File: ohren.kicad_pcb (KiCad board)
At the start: 2 copper layers, 60 x 28.7 mm, 34 parts, among them J1 Conn_01x14_Male, U1 TLC5951RHA, U2 TLC5951RHA

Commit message: Reroute finised
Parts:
- removed C4: CP, Capacitor_Tantalum_SMD:CP_EIA-6032-28_Kemet-C
- C10, C9: value CP -> C; footprint Capacitor_Tantalum_SMD:CP_EIA-6032-28_Kemet-C -> Capacitor_SMD:C_1206_3216Metric
- J1: value Conn_01x14_Male -> Conn_01x18_Male; footprint catear-pcb:solder_conn14 -> catear-pcb:solder_conn18
- moved C1 35.2 mm to (140.4, 107.9), turned to 270 degrees
- moved C3 28.1 mm to (138.4, 107.9), turned to 270 degrees
- moved C10 24.0 mm to (160.5, 112.6), turned to 180 degrees
- moved C9 15.1 mm to (128.0, 100.9)
- moved C6 13.8 mm to (145.6, 96.3), turned to 225 degrees
- moved C8 11.9 mm to (152.8, 102.3), turned to 225 degrees
- moved C7 10.7 mm to (135.4, 95.7)
- moved C5 8.68 mm to (122.9, 106.2)
- moved J1 3.55 mm to (139.2, 111.9), turned to 0 degrees
- turned D15 to 315 degrees
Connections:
- D19 pad 1: Net-(D19-Pad1) -> /U2_B4
- D20 pad 1: Net-(D20-Pad1) -> /U2_R4
- D21 pad 1: Net-(D21-Pad1) -> /U2_R1
- D23 pad 1: Net-(D23-Pad1) -> /U2_G1
- J1 pad 1: GND -> VCC
- J1 pad 10: /GSSIN -> /GSSCK
- J1 pad 11: /DCSIN -> /GSLAT
- J1 pad 12: GND -> /GSCKB
- J1 pad 13: VCC -> /DCSOUT
- J1 pad 14: VCC -> /GSSOUT
- J1 pad 2: /XBLNK -> VCC
- J1 pad 3: /DCSCK -> GND
- J1 pad 4: /GSSCK -> GND
- J1 pad 5: /GSLAT -> VDD
- J1 pad 6: /GSCKB -> /XBLNK
- J1 pad 7: VDD -> /DCSCK
- J1 pad 8: /DCSOUT -> /DCSIN
- J1 pad 9: /GSSOUT -> /GSSIN
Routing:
- net VCC: track 0.00 -> 157.2 mm, vias 0 -> 14
- net (no net): track 82.9 -> 0.00 mm, vias 4 -> 0
- net /U2_B6: track 0.00 -> 24.2 mm, vias 0 -> 1
- net /U2_G6: track 0.00 -> 22.8 mm, vias 0 -> 1
- net /U2_R6: track 0.00 -> 21.0 mm, vias 0 -> 1
- net /U2_G7: track 0.00 -> 15.2 mm, vias 0 -> 1
- net /U2_B5: track 0.00 -> 14.4 mm, vias 0 -> 1
- net /GSSOUT: track 0.00 -> 14.4 mm, vias 0 -> 1
- net /U2_B7: track 0.00 -> 13.7 mm, vias 0 -> 1
- net /U2_G5: track 0.00 -> 13.5 mm, vias 0 -> 1
- net /U2_R4: track 0.00 -> 13.5 mm, vias 0 -> 1
- net /DCSOUT: track 0.00 -> 13.2 mm, vias 0 -> 1
- net /U2_R5: track 0.00 -> 11.7 mm, vias 0 -> 1
- net /U2_R7: track 0.00 -> 11.6 mm, vias 0 -> 1
- net /GSSIN: track 0.00 -> 8.84 mm
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
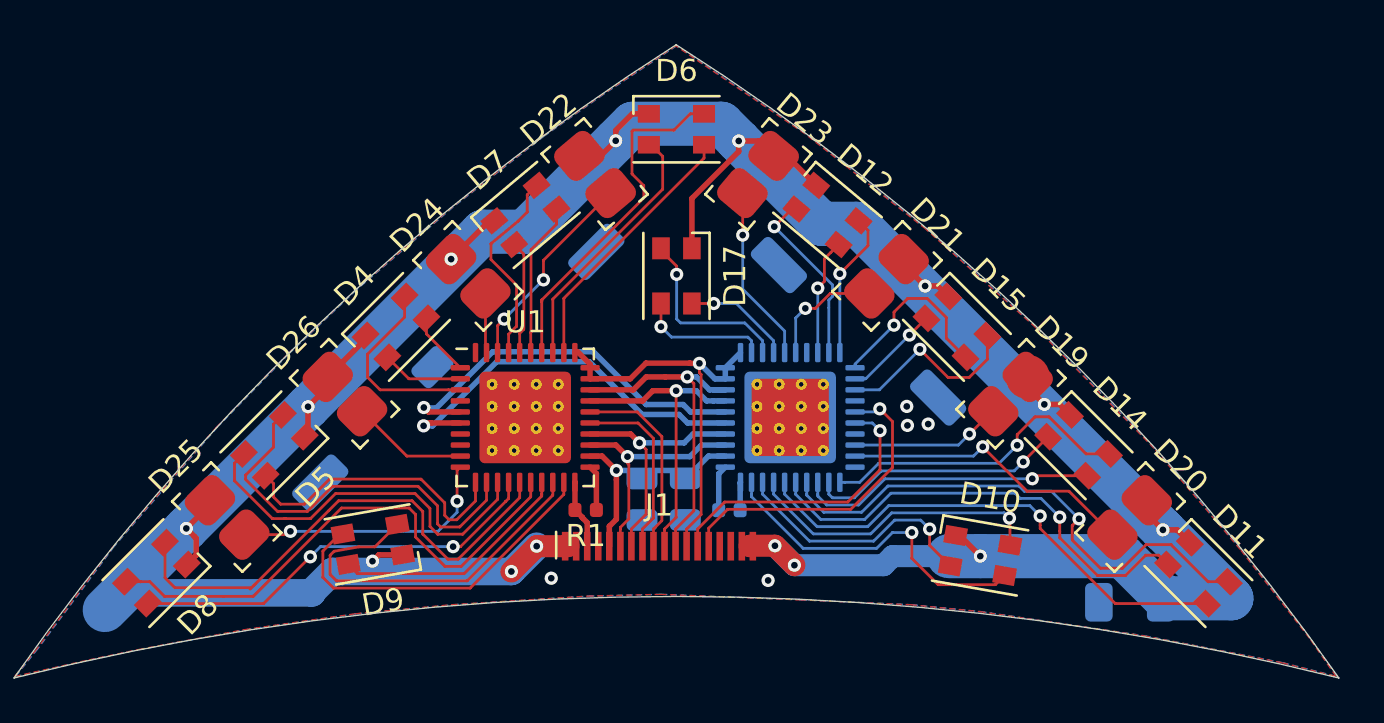
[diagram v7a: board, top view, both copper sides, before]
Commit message: Add additional VIA stitching and bypass capacitance
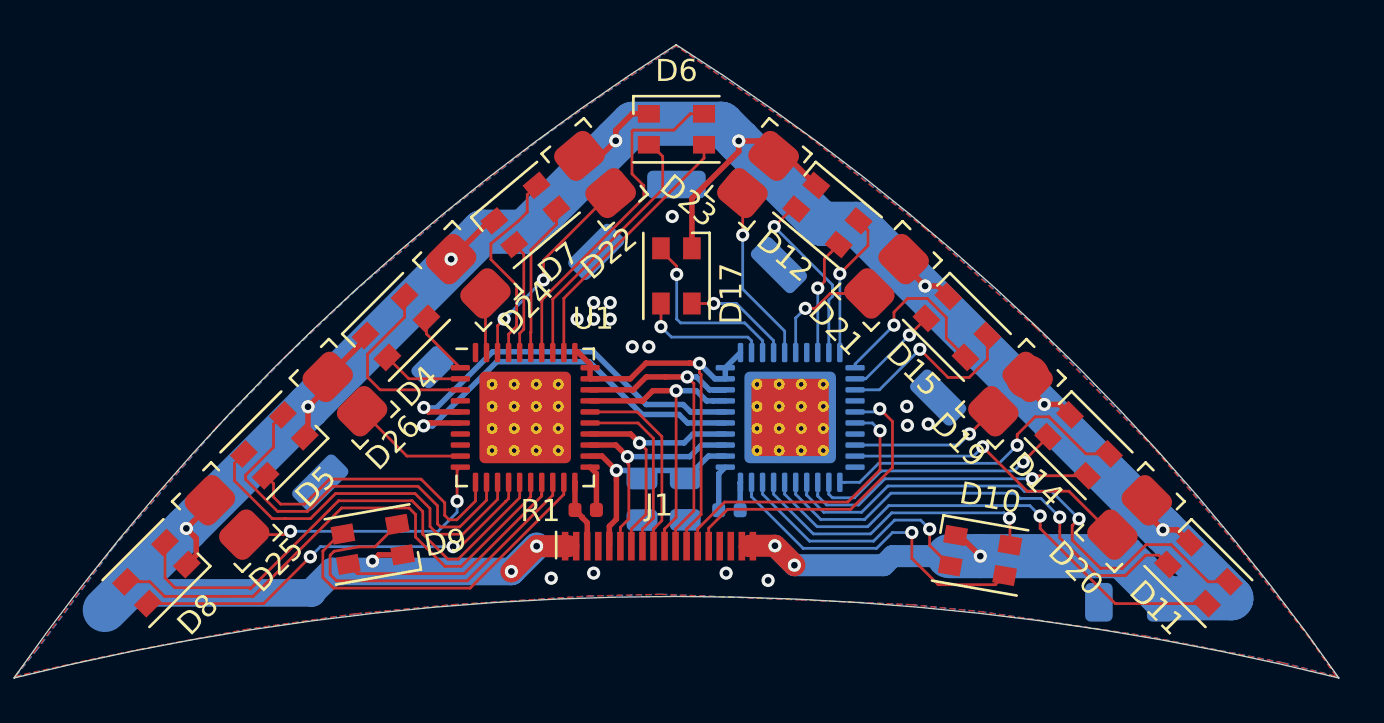
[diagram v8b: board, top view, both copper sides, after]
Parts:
- added C2: C, Capacitor_SMD:C_1210_3225Metric, B.Cu at (140.0, 92.2)
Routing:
- net GND: vias 5 -> 15
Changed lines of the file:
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@@
     (thickness 1.6)
     (drawings 9)
-    (tracks 605)
+    (tracks 615)
     (zones 0)
-    (modules 33)
+    (modules 34)
     (nets 69)
   )
@@
     (40 Dwgs.User user)
     (41 Cmts.User user)
-    (42 Eco1.User user hide)
-    (43 Eco2.User user hide)
+    (42 Eco1.User user)
+    (43 Eco2.User user)
     (44 Edge.Cuts user)
     (45 Margin user)
@@
     (pcbplotparams
       (layerselection 0x010fc_ffffffff)
-      (usegerberextensions false)
+      (usegerberextensions true)
       (usegerberattributes false)
       (usegerberadvancedattributes false)
@@
       (outputformat 1)
       (mirror false)
-      (drillshape 1)
+      (drillshape 0)
       (scaleselection 1)
-      (outputdirectory ""))
+      (outputdirectory "fab/"))
   )
   (net 0 "")
@@
     (add_net VDD)
   )
+  (module Capacitor_SMD:C_1210_3225Metric (layer B.Cu)
+    (at 140 92.25 270)
+    (descr "Capacitor SMD 1210 (3225 Metric), square (rectangular) end terminal, IPC_7351 nominal, (Body size source: http://www.tortai-tech.com/upload/download/2011102023233369053.pdf), generated with kicad-footprint-generator")
+    (tags capacitor)
+    (attr smd)
+    (fp_text reference C2 (at 0 2.28 270) (layer B.SilkS)
+      (effects (font (size 1 1) (thickness 0.15)) (justify mirror))
+    )
+    (fp_text value C (at 0 -2.28 270) (layer B.Fab)
+      (effects (font (size 1 1) (thickness 0.15)) (justify mirror))
+    )
+    (fp_text user %R (at 0 0 270) (layer B.Fab)
+      (effects (font (size 0.8 0.8) (thickness 0.12)) (justify mirror))
+    )
+    (fp_line (start 2.28 -1.58) (end -2.28 -1.58) (layer B.CrtYd) (width 0.05))
+    (fp_line (start 2.28 1.58) (end 2.28 -1.58) (layer B.CrtYd) (width 0.05))
+    (fp_line (start -2.28 1.58) (end 2.28 1.58) (layer B.CrtYd) (width 0.05))
+    (fp_line (start -2.28 -1.58) (end -2.28 1.58) (layer B.CrtYd) (width 0.05))
+    (fp_line (start -0.602064 -1.36) (end 0.602064 -1.36) (layer B.SilkS) (width 0.12))
+    (fp_line (start -0.602064 1.36) (end 0.602064 1.36) (layer B.SilkS) (width 0.12))
+    (fp_line (start 1.6 -1.25) (end -1.6 -1.25) (layer B.Fab) (width 0.1))
+    (fp_line (start 1.6 1.25) (end 1.6 -1.25) (layer B.Fab) (width 0.1))
+    (fp_line (start -1.6 1.25) (end 1.6 1.25) (layer B.Fab) (width 0.1))
+    (fp_line (start -1.6 -1.25) (end -1.6 1.25) (layer B.Fab) (width 0.1))
+    (pad 2 smd roundrect (at 1.4 0 270) (size 1.25 2.65) (layers B.Cu B.Paste B.Mask) (roundrect_rratio 0.2)
+      (net 31 GND))
+    (pad 1 smd roundrect (at -1.4 0 270) (size 1.25 2.65) (layers B.Cu B.Paste B.Mask) (roundrect_rratio 0.2)
+      (net 8 VCC))
+    (model ${KISYS3DMOD}/Capacitor_SMD.3dshapes/C_1210_3225Metric.wrl
+      (at (xyz 0 0 0))
+      (scale (xyz 1 1 1))
+      (rotate (xyz 0 0 0))
+    )
+  )
   (module Capacitor_SMD:C_1206_3216Metric (layer B.Cu)
     (at 160.53 112.57 180)
@@
   (module catear-pcb:smd_led_universal (layer F.Cu)
     (at 124.968 103.124 135)
-    (fp_text reference D26 (at 3.25 0 225) (layer F.SilkS)
+    (fp_text reference D26 (at -3.116927 -0.016971 225) (layer F.SilkS)
       (effects (font (size 1 1) (thickness 0.15)))
     )
@@
   (module catear-pcb:smd_led_universal (layer F.Cu)
     (at 119.634 108.712 135)
-    (fp_text reference D25 (at 3.25 0 225) (layer F.SilkS)
+    (fp_text reference D25 (at -3.114098 0.062225 225) (layer F.SilkS)
       (effects (font (size 1 1) (thickness 0.15)))
     )
@@
   (module catear-pcb:smd_led_universal (layer F.Cu)
     (at 130.556 97.79 135)
-    (fp_text reference D24 (at 3.25 0 225) (layer F.SilkS)
+    (fp_text reference D24 (at -2.887824 0.865499 225) (layer F.SilkS)
       (effects (font (size 1 1) (thickness 0.15)))
     )
@@
   (module catear-pcb:smd_led_universal (layer F.Cu)
     (at 143.71 93.1782 50)
-    (fp_text reference D23 (at 3.25 0 140) (layer F.SilkS)
+    (fp_text reference D23 (at -2.965929 -1.649431 140) (layer F.SilkS)
       (effects (font (size 1 1) (thickness 0.15)))
     )
@@
   (module catear-pcb:smd_led_universal (layer F.Cu)
     (at 136.296864 93.1782 130)
-    (fp_text reference D22 (at 3.25 0 220) (layer F.SilkS)
+    (fp_text reference D22 (at -3.157218 -1.809666 220) (layer F.SilkS)
       (effects (font (size 1 1) (thickness 0.15)))
     )
@@
   (module catear-pcb:smd_led_universal (layer F.Cu)
     (at 149.53 97.79 45)
-    (fp_text reference D21 (at 3.25 0 135) (layer F.SilkS)
+    (fp_text reference D21 (at -3.302189 0.049497 135) (layer F.SilkS)
       (effects (font (size 1 1) (thickness 0.15)))
     )
@@
   (module catear-pcb:smd_led_universal (layer F.Cu)
     (at 160.54 108.712 45)
-    (fp_text reference D20 (at 3.25 0 135) (layer F.SilkS)
+    (fp_text reference D20 (at -3.371485 -0.093338 135) (layer F.SilkS)
       (effects (font (size 1 1) (thickness 0.15)))
     )
@@
   (module catear-pcb:smd_led_universal (layer F.Cu)
     (at 155.145495 103.124 45)
-    (fp_text reference D19 (at 3.25 0 135) (layer F.SilkS)
+    (fp_text reference D19 (at -3.154753 -0.190562 135) (layer F.SilkS)
       (effects (font (size 1 1) (thickness 0.15)))
     )
@@
     (tags resistor)
     (attr smd)
-    (fp_text reference R1 (at 0 -1.17 180) (layer F.SilkS)
+    (fp_text reference R1 (at 2.05 -0.04 180) (layer F.SilkS)
       (effects (font (size 1 1) (thickness 0.15)))
     )
@@
     (tags capacitor)
     (attr smd)
-    (fp_text reference C3 (at 0 1.65 270) (layer B.SilkS)
+    (fp_text reference C3 (at -2.9175 -0.1 270) (layer B.SilkS)
       (effects (font (size 1 1) (thickness 0.15)) (justify mirror))
     )
@@
     (tags capacitor)
     (attr smd)
-    (fp_text reference C1 (at 0 1.65 270) (layer B.SilkS)
+    (fp_text reference C1 (at -2.83 0.01 270) (layer B.SilkS)
       (effects (font (size 1 1) (thickness 0.15)) (justify mirror))
     )
@@
     (tags "LED Cree PLCC-4")
     (attr smd)
-    (fp_text reference D17 (at 0 -2.65 270) (layer F.SilkS)
+    (fp_text reference D17 (at 0.8 -2.48 270) (layer F.SilkS)
       (effects (font (size 1 1) (thickness 0.15)))
     )
@@
     (tags "LED Cree PLCC-4")
     (attr smd)
-    (fp_text reference D15 (at 0 -2.65 315) (layer F.SilkS)
+    (fp_text reference D15 (at -0.028284 2.743574 315) (layer F.SilkS)
       (effects (font (size 1 1) (thickness 0.15)))
     )
@@
     (tags "LED Cree PLCC-4")
     (attr smd)
-    (fp_text reference D14 (at 0 -2.65 315) (layer F.SilkS)
+    (fp_text reference D14 (at -0.263208 2.453624 315) (layer F.SilkS)
       (effects (font (size 1 1) (thickness 0.15)))
     )
@@
     (tags "LED Cree PLCC-4")
     (attr smd)
-    (fp_text reference D12 (at 0 -2.65 320) (layer F.SilkS)
+    (fp_text reference D12 (at -0.295737 2.650102 320) (layer F.SilkS)
       (effects (font (size 1 1) (thickness 0.15)))
     )
@@
     (tags "LED Cree PLCC-4")
     (attr smd)
-    (fp_text reference D11 (at 0 -2.65 315) (layer F.SilkS)
+    (fp_text reference D11 (at -0.218432 2.438747 315) (layer F.SilkS)
       (effects (font (size 1 1) (thickness 0.15)))
     )
@@
     (tags "LED Cree PLCC-4")
     (attr smd)
-    (fp_text reference D9 (at 0 -2.650001 190) (layer F.SilkS)
+    (fp_text reference D9 (at -3.244061 -0.490781 190) (layer F.SilkS)
       (effects (font (size 1 1) (thickness 0.15)))
     )
@@
     (tags "LED Cree PLCC-4")
     (attr smd)
-    (fp_text reference D7 (at 0 -2.65 40) (layer F.SilkS)
+    (fp_text reference D7 (at -0.218838 2.609944 40) (layer F.SilkS)
       (effects (font (size 1 1) (thickness 0.15)))
     )
@@
     (tags "LED Cree PLCC-4")
     (attr smd)
-    (fp_text reference D4 (at 0 -2.65 45) (layer F.SilkS)
+    (fp_text reference D4 (at -1.216224 2.588011 45) (layer F.SilkS)
       (effects (font (size 1 1) (thickness 0.15)))
     )
@@
     (tags "QFN NoLead")
     (attr smd)
-    (fp_text reference U1 (at 0 -4.32) (layer F.SilkS)
+    (fp_text reference U1 (at 3.08 -4.48) (layer F.SilkS)
       (effects (font (size 1 1) (thickness 0.15)))
     )
@@
   (gr_arc (start 83 177) (end 170 116) (angle -22.52944362) (layer Edge.Cuts) (width 0.05))
   (gr_arc (start 140 236) (end 170 116) (angle -28.07248694) (layer Edge.Cuts) (width 0.05))
+  (via (at 142.25 111.25) (size 0.6) (drill 0.3) (layers F.Cu B.Cu) (net 31))
+  (via (at 136.25 111.25) (size 0.6) (drill 0.3) (layers F.Cu B.Cu) (net 31))
+  (via (at 137 99) (size 0.6) (drill 0.3) (layers F.Cu B.Cu) (net 31))
+  (via (at 135.5 99.75) (size 0.6) (drill 0.3) (layers F.Cu B.Cu) (net 31))
+  (via (at 136.25 99.75) (size 0.6) (drill 0.3) (layers F.Cu B.Cu) (net 31))
+  (via (at 137 99.75) (size 0.6) (drill 0.3) (layers F.Cu B.Cu) (net 31))
+  (via (at 138.75 101) (size 0.6) (drill 0.3) (layers F.Cu B.Cu) (net 31))
+  (via (at 138 101) (size 0.6) (drill 0.3) (layers F.Cu B.Cu) (net 31))
+  (via (at 136.25 99) (size 0.6) (drill 0.3) (layers F.Cu B.Cu) (net 31))
+  (via (at 139.81 95.1) (size 0.6) (drill 0.3) (layers F.Cu B.Cu) (net 31))
   (via (at 144.15 111.58) (size 0.6) (drill 0.3) (layers F.Cu B.Cu) (net 31))
   (via (at 134.33 111.48) (size 0.6) (drill 0.3) (layers F.Cu B.Cu) (net 31))
